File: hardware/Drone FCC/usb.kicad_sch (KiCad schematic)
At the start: 2 parts

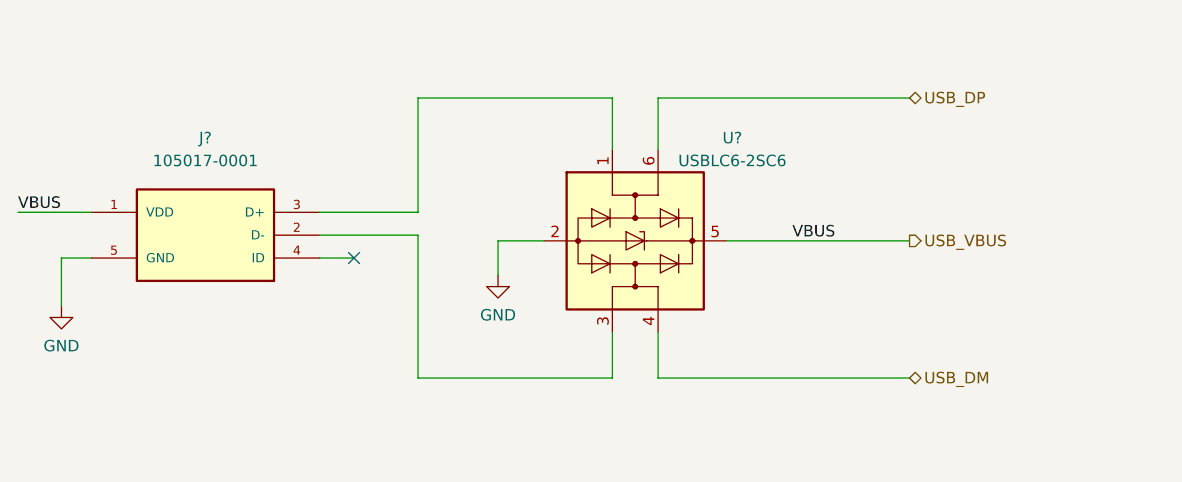
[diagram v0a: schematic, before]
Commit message: fix connection of TVS USB diode IC
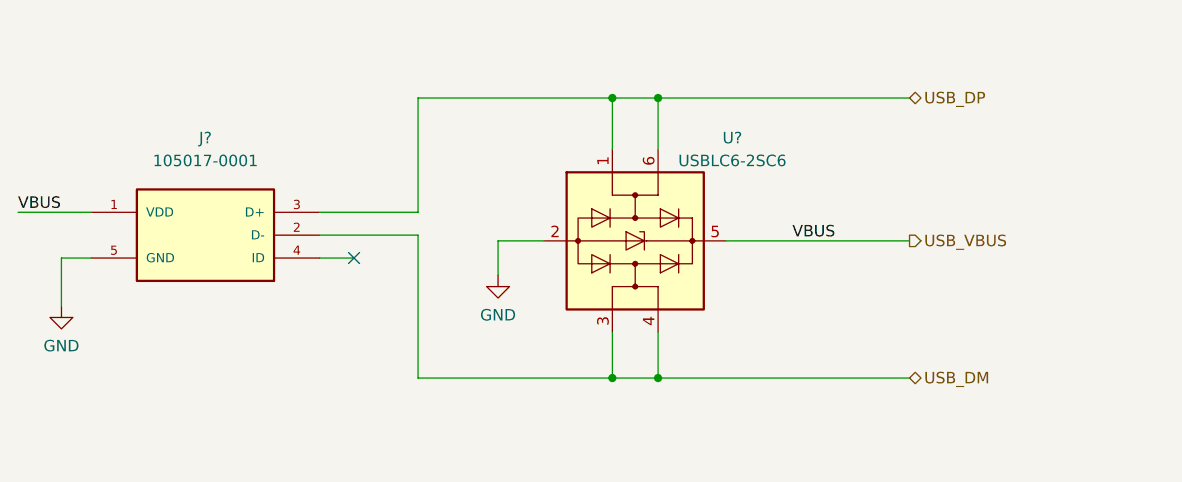
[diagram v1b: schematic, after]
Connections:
- net USB_DM: now also J?.2 (D-), U?.3 (I/O2)
- net USB_DP: now also J?.3 (D+), U?.1 (I/O1)
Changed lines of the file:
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@@
 (kicad_sch (version 20211123) (generator eeschema)
   (paper "A4")
+  (junction (at 128.27 104.775) (diameter 0) (color 0 0 0 0)
+  )
+  (junction (at 133.35 104.775) (diameter 0) (color 0 0 0 0)
+  )
+  (junction (at 128.27 73.66) (diameter 0) (color 0 0 0 0)
+  )
+  (junction (at 133.35 73.66) (diameter 0) (color 0 0 0 0)
+  )
   (no_connect (at 99.568 91.44))
   (wire (pts (xy 62.23 86.36) (xy 70.358 86.36))
@@
     (stroke (width 0) (type default) (color 0 0 0 0))
   )
-  (wire (pts (xy 133.35 104.775) (xy 161.29 104.775))
+  (wire (pts (xy 106.68 104.775) (xy 128.27 104.775))
+    (stroke (width 0) (type default) (color 0 0 0 0))
+  )
+  (wire (pts (xy 106.68 73.66) (xy 128.27 73.66))
     (stroke (width 0) (type default) (color 0 0 0 0))
   )
@@
     (stroke (width 0) (type default) (color 0 0 0 0))
   )
-  (wire (pts (xy 128.27 104.775) (xy 128.27 99.695))
-    (stroke (width 0) (type default) (color 0 0 0 0))
-  )
   (wire (pts (xy 95.758 88.9) (xy 106.68 88.9))
-    (stroke (width 0) (type default) (color 0 0 0 0))
-  )
-  (wire (pts (xy 106.68 104.775) (xy 128.27 104.775))
     (stroke (width 0) (type default) (color 0 0 0 0))
   )
@@
     (stroke (width 0) (type default) (color 0 0 0 0))
   )
-  (wire (pts (xy 133.35 79.375) (xy 133.35 73.66))
+  (wire (pts (xy 128.27 73.66) (xy 133.35 73.66))
+    (stroke (width 0) (type default) (color 0 0 0 0))
+  )
+  (wire (pts (xy 133.35 104.775) (xy 161.29 104.775))
+    (stroke (width 0) (type default) (color 0 0 0 0))
+  )
+  (wire (pts (xy 128.27 99.695) (xy 128.27 104.775))
+    (stroke (width 0) (type default) (color 0 0 0 0))
+  )
+  (wire (pts (xy 133.35 99.695) (xy 133.35 104.775))
     (stroke (width 0) (type default) (color 0 0 0 0))
   )
   (wire (pts (xy 133.35 73.66) (xy 161.29 73.66))
-    (stroke (width 0) (type default) (color 0 0 0 0))
-  )
-  (wire (pts (xy 128.27 73.66) (xy 128.27 79.375))
     (stroke (width 0) (type default) (color 0 0 0 0))
   )
@@
     (stroke (width 0) (type default) (color 0 0 0 0))
   )
-  (wire (pts (xy 133.35 99.695) (xy 133.35 104.775))
-    (stroke (width 0) (type default) (color 0 0 0 0))
-  )
   (wire (pts (xy 106.68 73.66) (xy 106.68 86.36))
     (stroke (width 0) (type default) (color 0 0 0 0))
   )
-  (wire (pts (xy 106.68 73.66) (xy 128.27 73.66))
+  (wire (pts (xy 128.27 104.775) (xy 133.35 104.775))
     (stroke (width 0) (type default) (color 0 0 0 0))
   )
+  (wire (pts (xy 133.35 73.66) (xy 133.35 79.375))
+    (stroke (width 0) (type default) (color 0 0 0 0))
+  )
+  (wire (pts (xy 128.27 73.66) (xy 128.27 79.375))
+    (stroke (width 0) (type default) (color 0 0 0 0))
+  )

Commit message: finish SWD functional schematic
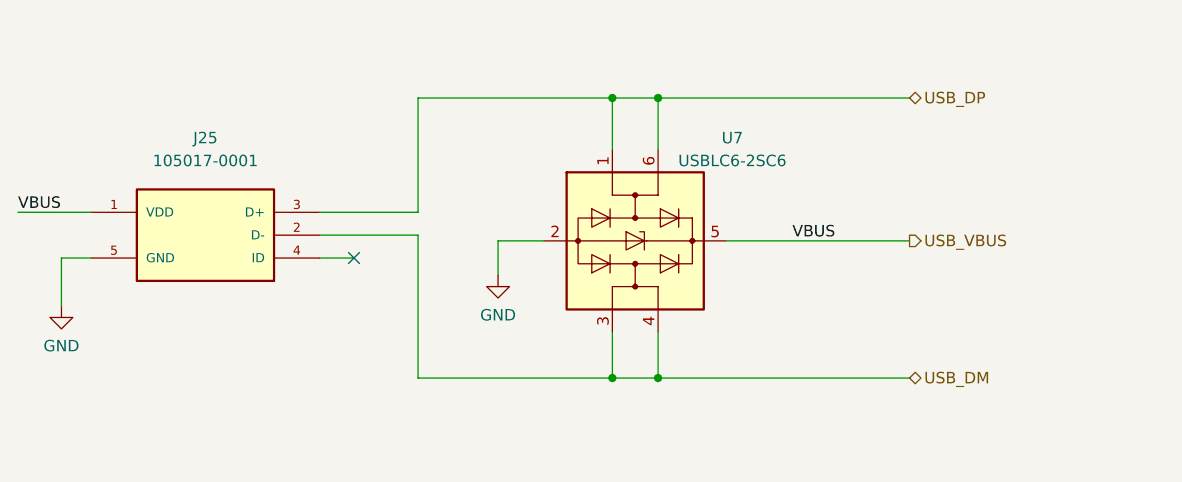
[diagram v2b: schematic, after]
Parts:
- gave numbers to parts that had none: 2
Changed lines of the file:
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@@
   (symbol (lib_id "power:GND") (at 115.57 93.345 0) (unit 1)
     (in_bom yes) (on_board yes) (fields_autoplaced)
-    (property "Reference" "#PWR?" (id 0) (at 115.57 99.695 0)
+    (property "Reference" "#PWR0125" (id 0) (at 115.57 99.695 0)
       (effects (font (size 1.27 1.27)) hide)
     )
@@
   (symbol (lib_id "105017-0001:105017-0001") (at 83.058 88.9 0) (mirror y) (unit 1)
     (in_bom yes) (on_board yes) (fields_autoplaced)
-    (property "Reference" "J?" (id 0) (at 83.058 78.105 0))
+    (property "Reference" "J25" (id 0) (at 83.058 78.105 0))
     (property "Value" "105017-0001" (id 1) (at 83.058 80.645 0))
     (property "Footprint" "105017-0001:MOLEX_105017-0001" (id 2) (at 83.058 88.9 0)
@@
   (symbol (lib_id "power:GND") (at 67.056 96.774 0) (unit 1)
     (in_bom yes) (on_board yes) (fields_autoplaced)
-    (property "Reference" "#PWR?" (id 0) (at 67.056 103.124 0)
+    (property "Reference" "#PWR0126" (id 0) (at 67.056 103.124 0)
       (effects (font (size 1.27 1.27)) hide)
     )
@@
   (symbol (lib_id "Power_Protection:USBLC6-2SC6") (at 130.81 89.535 270) (unit 1)
     (in_bom yes) (on_board yes)
-    (property "Reference" "U?" (id 0) (at 141.605 78.105 90))
+    (property "Reference" "U7" (id 0) (at 141.605 78.105 90))
     (property "Value" "USBLC6-2SC6" (id 1) (at 141.605 80.645 90))
     (property "Footprint" "Package_TO_SOT_SMD:SOT-23-6" (id 2) (at 118.11 89.535 0)

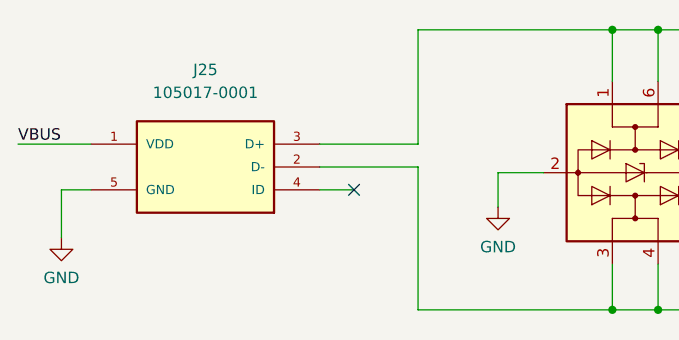
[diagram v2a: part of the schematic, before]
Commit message: add external communication connectors
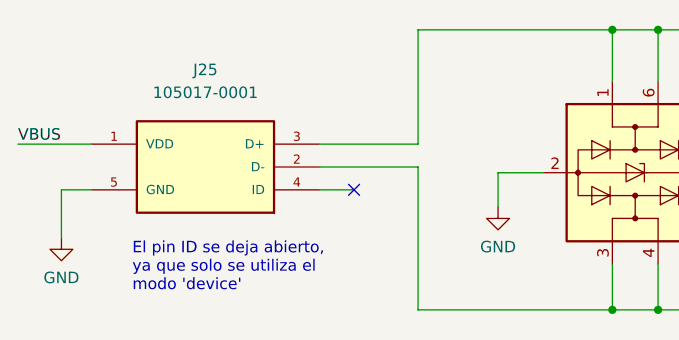
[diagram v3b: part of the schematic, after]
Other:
- note added: "El pin ID se deja abierto, ya que solo se utiliza el modo 'device'"
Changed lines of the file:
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@@
     (stroke (width 0) (type default) (color 0 0 0 0))
+  )
+  (text "El pin ID se deja abierto,\nya que solo se utiliza el\nmodo 'device'"
+    (at 74.93 102.87 0)
+    (effects (font (size 1.27 1.27)) (justify left bottom))
   )
   (label "VBUS" (at 62.23 86.36 0)

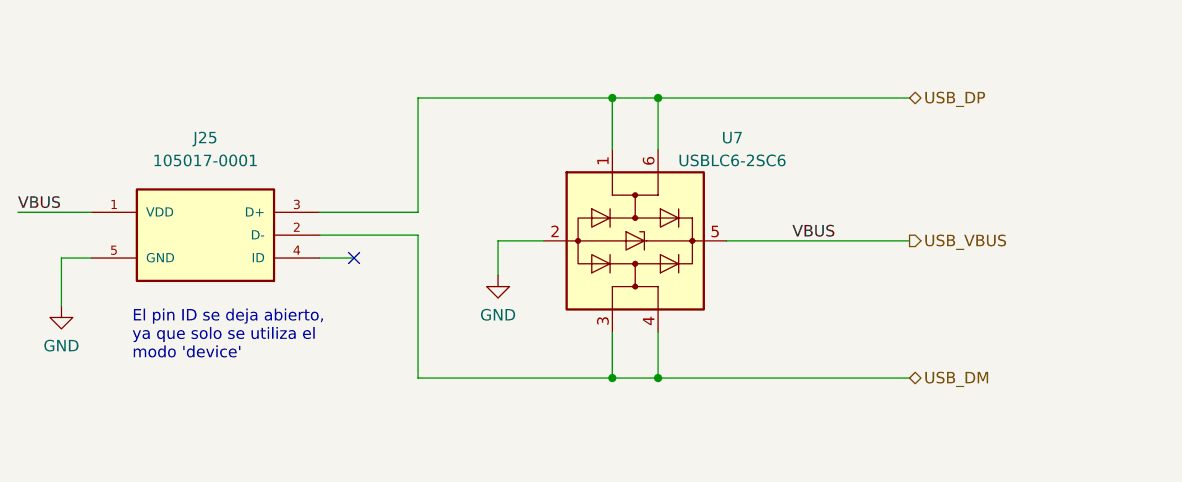
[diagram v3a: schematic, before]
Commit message: re enumeration of components
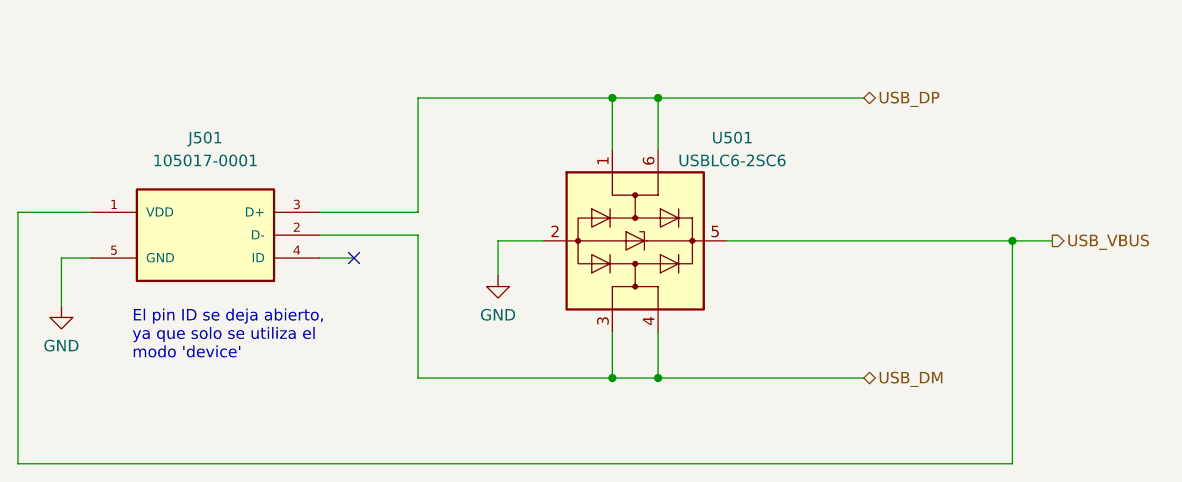
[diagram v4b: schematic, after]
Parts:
- renumbered J25 to J501, U7 to U501
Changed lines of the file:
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@@
 (kicad_sch (version 20211123) (generator eeschema)
   (paper "A4")
+  (junction (at 133.35 104.775) (diameter 0) (color 0 0 0 0)
+  )
   (junction (at 128.27 104.775) (diameter 0) (color 0 0 0 0)
   )
-  (junction (at 133.35 104.775) (diameter 0) (color 0 0 0 0)
+  (junction (at 172.72 89.535) (diameter 0) (color 0 0 0 0)
+  )
+  (junction (at 133.35 73.66) (diameter 0) (color 0 0 0 0)
   )
   (junction (at 128.27 73.66) (diameter 0) (color 0 0 0 0)
-  )
-  (junction (at 133.35 73.66) (diameter 0) (color 0 0 0 0)
   )
   (no_connect (at 99.568 91.44))
@@
     (stroke (width 0) (type default) (color 0 0 0 0))
   )
+  (wire (pts (xy 133.35 104.775) (xy 156.21 104.775))
+    (stroke (width 0) (type default) (color 0 0 0 0))
+  )
   (wire (pts (xy 106.68 88.9) (xy 106.68 104.775))
     (stroke (width 0) (type default) (color 0 0 0 0))
@@
     (stroke (width 0) (type default) (color 0 0 0 0))
   )
+  (wire (pts (xy 62.23 114.3) (xy 62.23 86.36))
+    (stroke (width 0) (type default) (color 0 0 0 0))
+  )
   (wire (pts (xy 128.27 73.66) (xy 133.35 73.66))
     (stroke (width 0) (type default) (color 0 0 0 0))
   )
-  (wire (pts (xy 133.35 104.775) (xy 161.29 104.775))
+  (wire (pts (xy 133.35 73.66) (xy 156.21 73.66))
+    (stroke (width 0) (type default) (color 0 0 0 0))
+  )
+  (wire (pts (xy 172.72 114.3) (xy 62.23 114.3))
+    (stroke (width 0) (type default) (color 0 0 0 0))
+  )
+  (wire (pts (xy 172.72 89.535) (xy 177.165 89.535))
     (stroke (width 0) (type default) (color 0 0 0 0))
   )
@@
     (stroke (width 0) (type default) (color 0 0 0 0))
   )
-  (wire (pts (xy 133.35 73.66) (xy 161.29 73.66))
+  (wire (pts (xy 172.72 89.535) (xy 172.72 114.3))
     (stroke (width 0) (type default) (color 0 0 0 0))
   )
@@
     (stroke (width 0) (type default) (color 0 0 0 0))
   )
-  (wire (pts (xy 140.97 89.535) (xy 161.29 89.535))
+  (wire (pts (xy 140.97 89.535) (xy 172.72 89.535))
     (stroke (width 0) (type default) (color 0 0 0 0))
   )
@@
     (effects (font (size 1.27 1.27)) (justify left bottom))
   )
-  (label "VBUS" (at 62.23 86.36 0)
-    (effects (font (size 1.27 1.27)) (justify left bottom))
-  )
-  (label "VBUS" (at 153.035 89.535 180)
-    (effects (font (size 1.27 1.27)) (justify right bottom))
-  )
-  (hierarchical_label "USB_DP" (shape bidirectional) (at 161.29 73.66 0)
+  (hierarchical_label "USB_DP" (shape bidirectional) (at 156.21 73.66 0)
     (effects (font (size 1.27 1.27)) (justify left))
   )
-  (hierarchical_label "USB_VBUS" (shape output) (at 161.29 89.535 0)
+  (hierarchical_label "USB_VBUS" (shape output) (at 177.165 89.535 0)
     (effects (font (size 1.27 1.27)) (justify left))
   )
-  (hierarchical_label "USB_DM" (shape bidirectional) (at 161.29 104.775 0)
+  (hierarchical_label "USB_DM" (shape bidirectional) (at 156.21 104.775 0)
     (effects (font (size 1.27 1.27)) (justify left))
   )
@@
   (symbol (lib_id "105017-0001:105017-0001") (at 83.058 88.9 0) (mirror y) (unit 1)
     (in_bom yes) (on_board yes) (fields_autoplaced)
-    (property "Reference" "J25" (id 0) (at 83.058 78.105 0))
+    (property "Reference" "J501" (id 0) (at 83.058 78.105 0))
     (property "Value" "105017-0001" (id 1) (at 83.058 80.645 0))
     (property "Footprint" "105017-0001:MOLEX_105017-0001" (id 2) (at 83.058 88.9 0)
@@
   (symbol (lib_id "Power_Protection:USBLC6-2SC6") (at 130.81 89.535 270) (unit 1)
     (in_bom yes) (on_board yes)
-    (property "Reference" "U7" (id 0) (at 141.605 78.105 90))
+    (property "Reference" "U501" (id 0) (at 141.605 78.105 90))
     (property "Value" "USBLC6-2SC6" (id 1) (at 141.605 80.645 90))
     (property "Footprint" "Package_TO_SOT_SMD:SOT-23-6" (id 2) (at 118.11 89.535 0)

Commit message: start routing
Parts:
- J501: value 105017-0001 -> Micro USB - B
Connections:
- net GND: now also J501.6 (SHIELD), J501.7 (MOUNT_2)
- net USB_DM: now also J501.3 (D+); no longer J501.2 (D-)
- net USB_DP: now also J501.2 (D-); no longer J501.3 (D+)
- no-connect marks 1 -> 2
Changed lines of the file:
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@@
 (kicad_sch (version 20211123) (generator eeschema)
   (paper "A4")
+  (junction (at 168.275 89.535) (diameter 0) (color 0 0 0 0)
+  )
   (junction (at 133.35 104.775) (diameter 0) (color 0 0 0 0)
   )
   (junction (at 128.27 104.775) (diameter 0) (color 0 0 0 0)
   )
-  (junction (at 172.72 89.535) (diameter 0) (color 0 0 0 0)
+  (junction (at 133.35 73.66) (diameter 0) (color 0 0 0 0)
   )
-  (junction (at 133.35 73.66) (diameter 0) (color 0 0 0 0)
+  (junction (at 102.235 96.52) (diameter 0) (color 0 0 0 0)
+  )
+  (junction (at 102.235 99.06) (diameter 0) (color 0 0 0 0)
   )
   (junction (at 128.27 73.66) (diameter 0) (color 0 0 0 0)
   )
   (no_connect (at 99.568 91.44))
-  (wire (pts (xy 62.23 86.36) (xy 70.358 86.36))
-    (stroke (width 0) (type default) (color 0 0 0 0))
-  )
+  (no_connect (at 99.695 101.6))
   (wire (pts (xy 120.65 89.535) (xy 115.57 89.535))
     (stroke (width 0) (type default) (color 0 0 0 0))
   )
-  (wire (pts (xy 95.758 91.44) (xy 99.568 91.44))
+  (wire (pts (xy 95.25 91.44) (xy 99.568 91.44))
     (stroke (width 0) (type default) (color 0 0 0 0))
   )
@@
     (stroke (width 0) (type default) (color 0 0 0 0))
   )
+  (wire (pts (xy 100.33 83.82) (xy 100.33 64.77))
+    (stroke (width 0) (type default) (color 0 0 0 0))
+  )
   (wire (pts (xy 106.68 73.66) (xy 128.27 73.66))
     (stroke (width 0) (type default) (color 0 0 0 0))
   )
-  (wire (pts (xy 95.758 86.36) (xy 106.68 86.36))
+  (wire (pts (xy 100.33 64.77) (xy 168.275 64.77))
     (stroke (width 0) (type default) (color 0 0 0 0))
   )
-  (wire (pts (xy 95.758 88.9) (xy 106.68 88.9))
+  (wire (pts (xy 95.25 88.9) (xy 106.68 88.9))
+    (stroke (width 0) (type default) (color 0 0 0 0))
+  )
+  (wire (pts (xy 102.235 96.52) (xy 102.235 99.06))
     (stroke (width 0) (type default) (color 0 0 0 0))
   )
@@
     (stroke (width 0) (type default) (color 0 0 0 0))
   )
-  (wire (pts (xy 70.358 91.44) (xy 67.056 91.44))
+  (wire (pts (xy 95.25 86.36) (xy 106.68 86.36))
     (stroke (width 0) (type default) (color 0 0 0 0))
   )
   (wire (pts (xy 115.57 89.535) (xy 115.57 93.345))
-    (stroke (width 0) (type default) (color 0 0 0 0))
-  )
-  (wire (pts (xy 62.23 114.3) (xy 62.23 86.36))
     (stroke (width 0) (type default) (color 0 0 0 0))
   )
@@
     (stroke (width 0) (type default) (color 0 0 0 0))
   )
-  (wire (pts (xy 172.72 114.3) (xy 62.23 114.3))
+  (wire (pts (xy 95.25 96.52) (xy 102.235 96.52))
     (stroke (width 0) (type default) (color 0 0 0 0))
   )
-  (wire (pts (xy 172.72 89.535) (xy 177.165 89.535))
+  (wire (pts (xy 95.25 99.06) (xy 102.235 99.06))
+    (stroke (width 0) (type default) (color 0 0 0 0))
+  )
+  (wire (pts (xy 102.235 93.98) (xy 102.235 96.52))
+    (stroke (width 0) (type default) (color 0 0 0 0))
+  )
+  (wire (pts (xy 95.25 101.6) (xy 99.695 101.6))
     (stroke (width 0) (type default) (color 0 0 0 0))
   )
@@
     (stroke (width 0) (type default) (color 0 0 0 0))
   )
-  (wire (pts (xy 172.72 89.535) (xy 172.72 114.3))
+  (wire (pts (xy 102.235 99.06) (xy 102.235 104.775))
     (stroke (width 0) (type default) (color 0 0 0 0))
   )
-  (wire (pts (xy 67.056 91.44) (xy 67.056 96.774))
+  (wire (pts (xy 140.97 89.535) (xy 168.275 89.535))
     (stroke (width 0) (type default) (color 0 0 0 0))
   )
-  (wire (pts (xy 140.97 89.535) (xy 172.72 89.535))
+  (wire (pts (xy 168.275 89.535) (xy 177.165 89.535))
     (stroke (width 0) (type default) (color 0 0 0 0))
   )
@@
     (stroke (width 0) (type default) (color 0 0 0 0))
   )
+  (wire (pts (xy 95.25 83.82) (xy 100.33 83.82))
+    (stroke (width 0) (type default) (color 0 0 0 0))
+  )
+  (wire (pts (xy 95.25 93.98) (xy 102.235 93.98))
+    (stroke (width 0) (type default) (color 0 0 0 0))
+  )
+  (wire (pts (xy 168.275 64.77) (xy 168.275 89.535))
+    (stroke (width 0) (type default) (color 0 0 0 0))
+  )
   (text "El pin ID se deja abierto,\nya que solo se utiliza el\nmodo 'device'"
-    (at 74.93 102.87 0)
+    (at 71.755 111.125 0)
     (effects (font (size 1.27 1.27)) (justify left bottom))
   )
@@
     (pin "1")
   )
-  (symbol (lib_id "105017-0001:105017-0001") (at 83.058 88.9 0) (mirror y) (unit 1)
+  (symbol (lib_name "105017-0001_1") (lib_id "105017-0001:105017-0001") (at 82.55 95.25 0) (unit 1)
     (in_bom yes) (on_board yes) (fields_autoplaced)
-    (property "Reference" "J501" (id 0) (at 83.058 78.105 0))
-    (property "Value" "105017-0001" (id 1) (at 83.058 80.645 0))
-    (property "Footprint" "105017-0001:MOLEX_105017-0001" (id 2) (at 83.058 88.9 0)
+    (property "Reference" "J501" (id 0) (at 82.55 76.2 0))
+    (property "Value" "Micro USB - B" (id 1) (at 82.55 78.74 0))
+    (property "Footprint" "105017-0001:MOLEX_105017-0001" (id 2) (at 82.55 110.49 0)
       (effects (font (size 1.27 1.27)) (justify bottom) hide)
     )
-    (property "Datasheet" "" (id 3) (at 83.058 88.9 0)
+    (property "Datasheet" "" (id 3) (at 82.55 95.25 0)
       (effects (font (size 1.27 1.27)) hide)
     )
@@
     (pin "4")
     (pin "5")
+    (pin "6")
+    (pin "7")
+    (pin "7")
   )
-  (symbol (lib_id "power:GND") (at 67.056 96.774 0) (unit 1)
+  (symbol (lib_id "power:GND") (at 102.235 104.775 0) (mirror y) (unit 1)
     (in_bom yes) (on_board yes) (fields_autoplaced)
-    (property "Reference" "#PWR0126" (id 0) (at 67.056 103.124 0)
+    (property "Reference" "#PWR0126" (id 0) (at 102.235 111.125 0)
       (effects (font (size 1.27 1.27)) hide)
     )
-    (property "Value" "GND" (id 1) (at 67.056 101.219 0))
-    (property "Footprint" "" (id 2) (at 67.056 96.774 0)
+    (property "Value" "GND" (id 1) (at 102.235 109.22 0))
+    (property "Footprint" "" (id 2) (at 102.235 104.775 0)
       (effects (font (size 1.27 1.27)) hide)
     )
-    (property "Datasheet" "" (id 3) (at 67.056 96.774 0)
+    (property "Datasheet" "" (id 3) (at 102.235 104.775 0)
       (effects (font (size 1.27 1.27)) hide)
     )
